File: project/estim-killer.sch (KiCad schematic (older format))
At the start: 11 parts

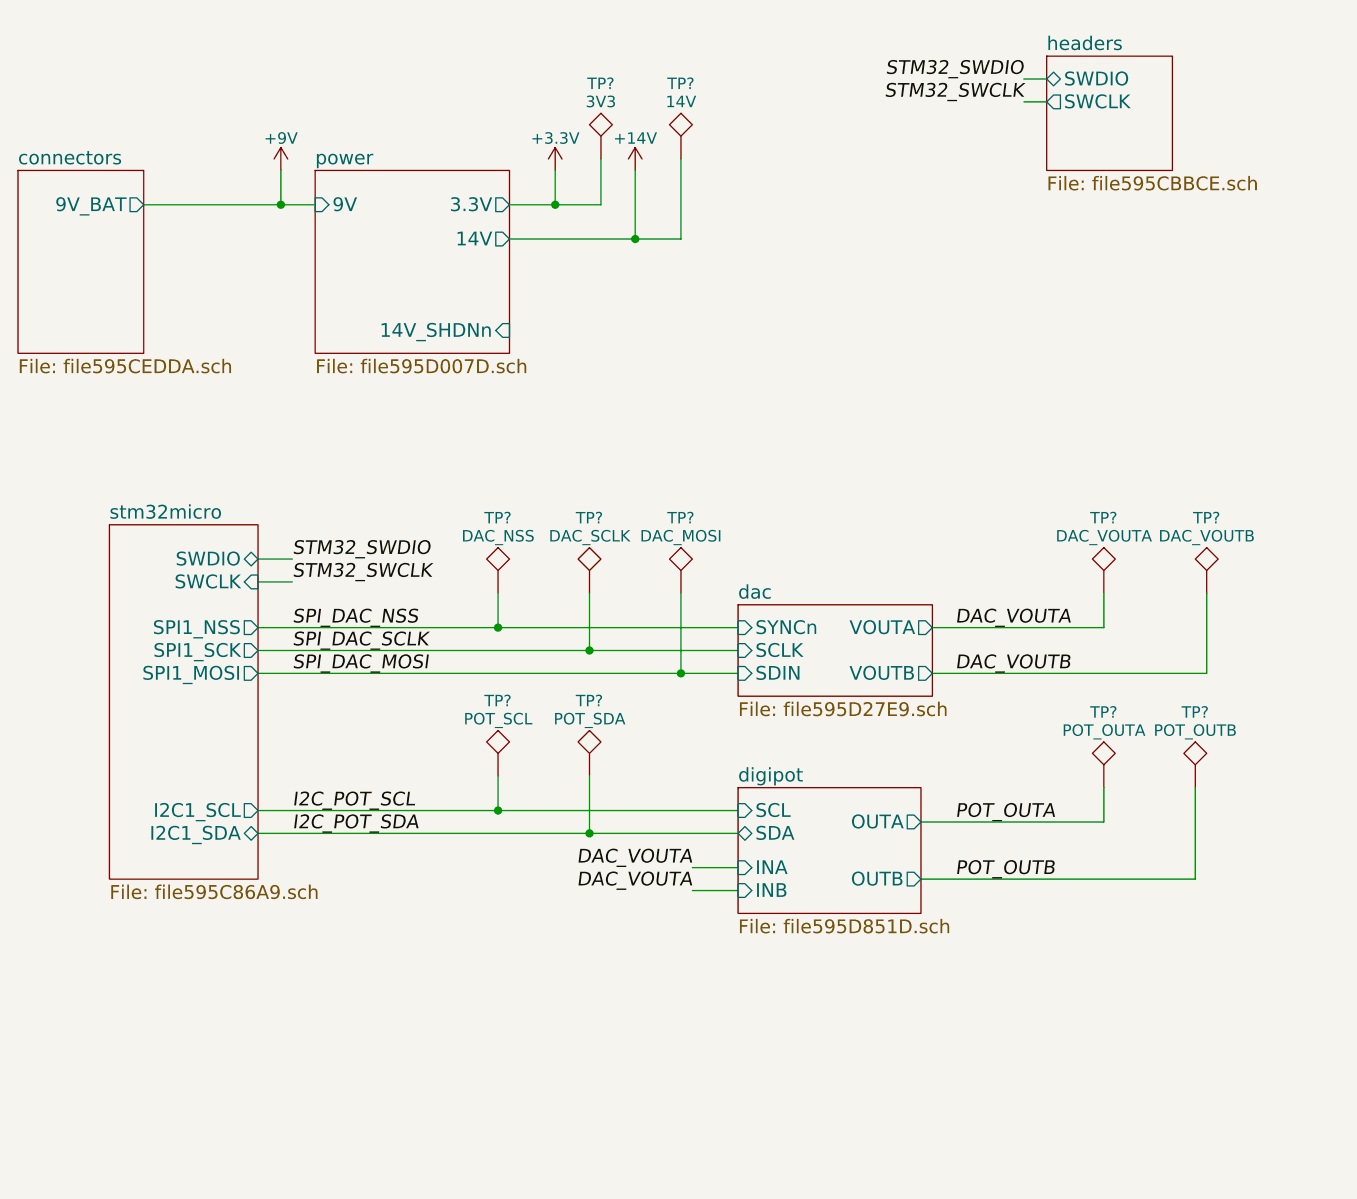
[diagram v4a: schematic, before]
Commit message: Add output amplifier (LM4952) to schematic.
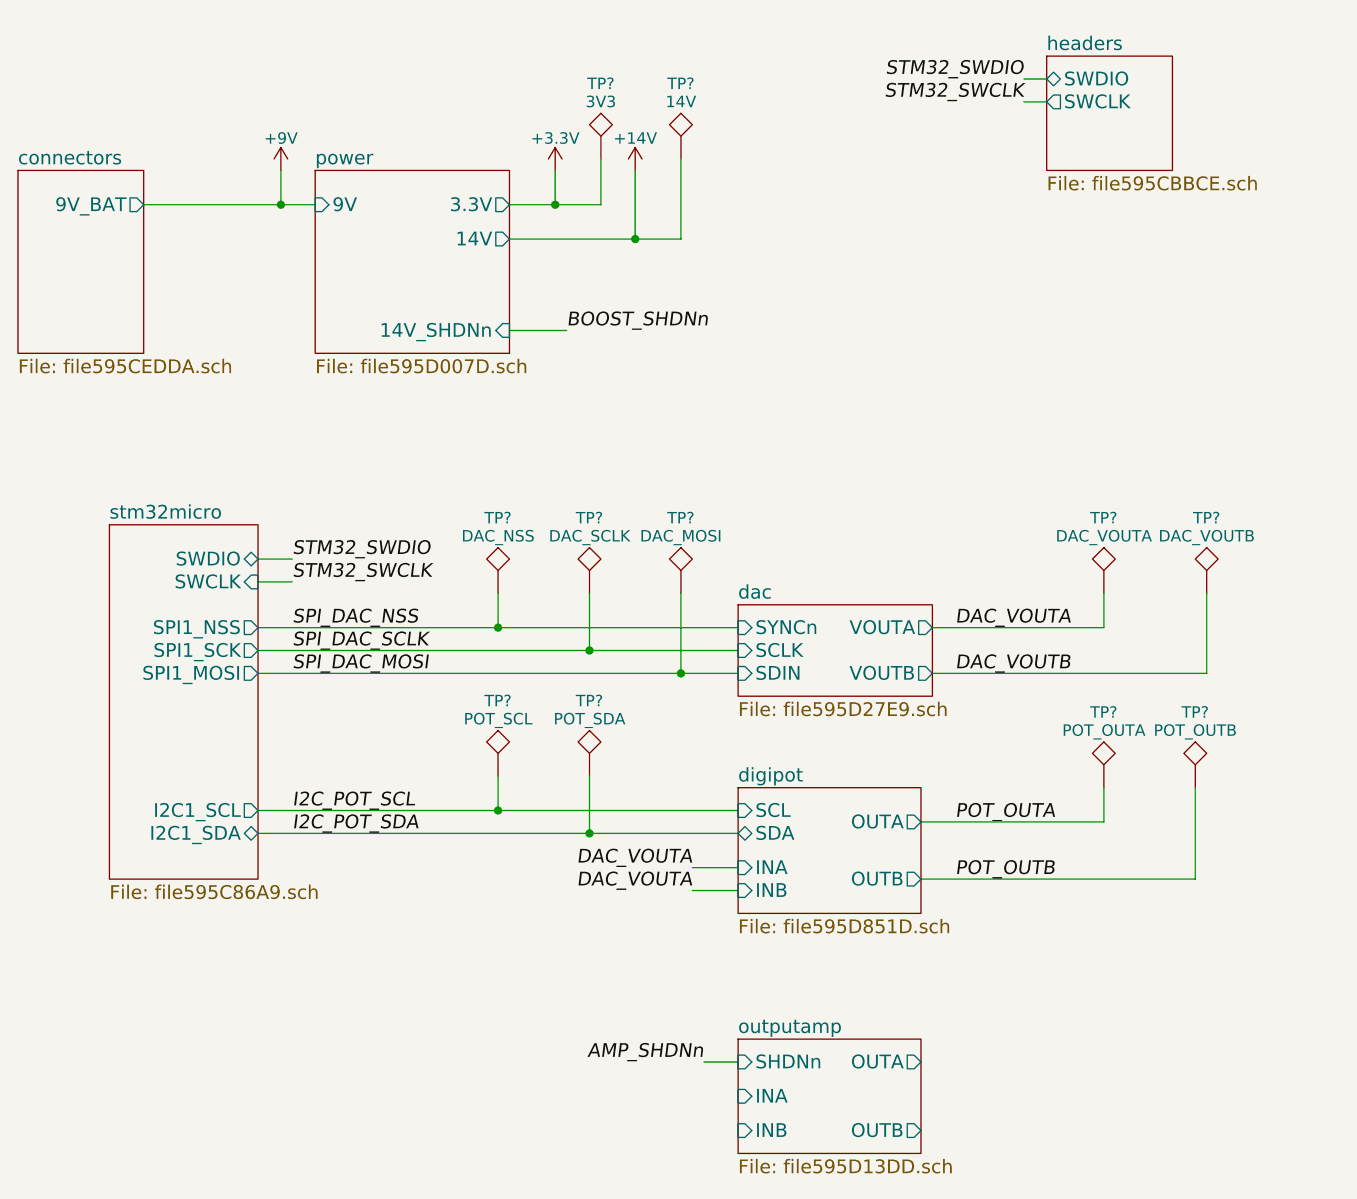
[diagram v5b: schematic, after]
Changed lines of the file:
@@
 $Descr A4 11693 8268
 encoding utf-8
-Sheet 1 7
+Sheet 1 8
 Title ""
 Date ""
@@
 	5250 950  5350 950
 Wire Wire Line
-	1400 1500 2150 1500
+	1400 1500 2000 1500
+Wire Wire Line
+	2000 1500 2150 1500
 Wire Wire Line
 	2000 1350 2000 1500
 Connection ~ 2000 1500
 Wire Wire Line
-	3000 1500 3400 1500
+	3000 1500 3200 1500
+Wire Wire Line
+	3200 1500 3400 1500
 Wire Wire Line
 	3400 1500 3400 1300
@@
 Connection ~ 3200 1500
 Wire Wire Line
-	1900 3350 4000 3350
-Wire Wire Line
-	1900 3450 4000 3450
-Wire Wire Line
-	1900 3550 4000 3550
+	1900 3350 2950 3350
+Wire Wire Line
+	2950 3350 4000 3350
+Wire Wire Line
+	1900 3450 3350 3450
+Wire Wire Line
+	3350 3450 4000 3450
+Wire Wire Line
+	1900 3550 3750 3550
+Wire Wire Line
+	3750 3550 4000 3550
 Wire Wire Line
 	2950 3200 2950 3350
@@
 	6050 3550 6050 3200
 Wire Wire Line
-	1900 4150 4000 4150
-Wire Wire Line
-	1900 4250 4000 4250
+	1900 4150 2950 4150
+Wire Wire Line
+	2950 4150 4000 4150
+Wire Wire Line
+	1900 4250 3350 4250
+Wire Wire Line
+	3350 4250 4000 4250
 Wire Wire Line
 	2950 4000 2950 4150
@@
 	6000 4450 6000 4050
 Wire Wire Line
-	3000 1650 3750 1650
+	3000 1650 3550 1650
+Wire Wire Line
+	3550 1650 3750 1650
 Wire Wire Line
 	3750 1650 3750 1300
@@
 	3550 1350 3550 1650
 Connection ~ 3550 1650
+$Sheet
+S 4000 5150 800  500
+U 595D13DE
+F0 "outputamp" 60
+F1 "file595D13DD.sch" 60
+F2 "SHDNn" I L 4000 5250 60
+F3 "INA" I L 4000 5400 60
+F4 "INB" I L 4000 5550 60
+F5 "OUTA" O R 4800 5250 60
+F6 "OUTB" O R 4800 5550 60
+$EndSheet
+Text Label 3250 2050 0    60   Italic 0
+BOOST_SHDNn
+Wire Wire Line
+	3250 2050 3000 2050
+Text Label 3850 5250 2    60   Italic 0
+AMP_SHDNn
+Wire Wire Line
+	3850 5250 4000 5250
 $EndSCHEMATC
